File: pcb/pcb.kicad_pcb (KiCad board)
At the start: 2 copper layers, 95.2 x 71.1 mm, 14 parts, among them J1 encoder, J2 programmer, J3 oled display, J4 usb-ttl, SW1 reset, U1 ATmega32-16P

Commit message: actualizacion de pcb
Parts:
- added R3: 330, Resistor_THT:R_Axial_DIN0207_L6.3mm_D2.5mm_P7.62mm_Horizontal, F.Cu at (131.0, 73.0)
- added R4: 330, Resistor_THT:R_Axial_DIN0207_L6.3mm_D2.5mm_P7.62mm_Horizontal, F.Cu at (113.0, 72.8)
- added R5: 330, Resistor_THT:R_Axial_DIN0207_L6.3mm_D2.5mm_P7.62mm_Horizontal, F.Cu at (149.0, 72.8)
- added SW2: play/pause, Button_Switch_THT:SW_PUSH_6mm, F.Cu at (120.5, 66.8)
- added SW3: prev track, Button_Switch_THT:SW_PUSH_6mm, F.Cu at (101.8, 66.8)
- added SW4: next track, Button_Switch_THT:SW_PUSH_6mm, F.Cu at (138.5, 66.8)
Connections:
- J1 pad 3: unconnected-(J1-Pin_3-Pad3) -> Net-(J1-Pin_3)
- U1 pad 18: unconnected-(U1-PD4-Pad18) -> Net-(J1-Pin_3)
- U1 pad 21: unconnected-(U1-PD7-Pad21) -> Net-(U1-PD7)
- U1 pad 22: unconnected-(U1-PC0-Pad22) -> Net-(U1-PC0)
- U1 pad 23: unconnected-(U1-PC1-Pad23) -> Net-(U1-PC1)
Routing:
- net +5V: track 146.0 -> 213.8 mm
- net Net-(U1-PC1): track 0.00 -> 48.6 mm
- net Net-(U1-PC0): track 0.00 -> 32.4 mm
- net Net-(U1-PD7): track 0.00 -> 23.4 mm
- net Net-(J1-Pin_3): track 0.00 -> 18.0 mm

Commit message: add oled footprint
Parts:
- removed J3: oled display, Connector_PinHeader_2.54mm:PinHeader_1x20_P2.54mm_Vertical
- added DS1: NHD-0420CW-AG3, Library:NHD-0420CW-AG3, F.Cu at (107.3, 107.2)
- moved REF** 140.6 mm to (302.9, 143.9)
- moved REF** 140.3 mm to (304.1, 65.9)
- moved C1 108.4 mm to (237.6, 112.7)
- moved D1 108.4 mm to (265.5, 120.3)
- moved J1 108.4 mm to (255.3, 120.3)
- moved J4 108.4 mm to (245.2, 122.9)
- moved R3 108.4 mm to (239.0, 81.6)
- moved R4 108.4 mm to (221.0, 81.4)
- moved SW1 108.4 mm to (210.7, 128.2)
- moved SW2 108.4 mm to (228.5, 75.3)
- moved SW3 108.4 mm to (209.8, 75.3)
- moved SW4 108.4 mm to (246.5, 75.3)
- moved U1 108.4 mm to (209.6, 108.5)
- moved J2 108.4 mm to (222.3, 112.7)
- moved R2 108.4 mm to (232.5, 126.7)
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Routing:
- removed copper zone on B.Cu, net GND
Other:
- board size 95.2 x 71.1 mm -> 295 x 93 mm

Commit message: actualizacion de archivos con footprint OLED
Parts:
- moved J1 27.8 mm to (264.2, 94.0)
- moved REF** 4.67 mm to (19.9, 63.9)
- moved J2 4.20 mm to (218.4, 114.3)
- moved U1 3.95 mm to (205.7, 109.2)
- moved REF** 3.74 mm to (304.3, 147.3)
- moved DS1 3.55 mm to (110.5, 105.7)
- moved REF** 2.94 mm to (20.3, 146.9)
- moved D1 2.09 mm to (264.2, 121.9)
- moved C1 2.00 mm to (238.8, 114.3)
- moved J4 2.00 mm to (246.4, 124.5)
- moved REF** 1.98 mm to (304.4, 63.9)
- moved R2 1.64 mm to (231.1, 125.7)
- moved R3 1.59 mm to (238.7, 80.0)
- moved R1 1.52 mm to (259.1, 111.8)
- moved R4 1.41 mm to (220.7, 80.0)
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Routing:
- net Net-(DS1-~{CS}): track 20.3 -> 116.6 mm
- net Net-(DS1-DB1): track 35.3 -> 114.0 mm
- net Net-(DS1-DB0): track 38.5 -> 114.0 mm
- net +5V: track 213.8 -> 279.2 mm
- net GND: track 22.8 -> 0.00 mm
- net Net-(J1-Pin_3): track 18.0 -> 25.7 mm
- net Net-(J2-Pin_4): track 58.1 -> 54.2 mm
- net Net-(D1-A): track 5.08 -> 8.67 mm
- net Net-(J4-Pin_2): track 14.4 -> 17.3 mm
- net Net-(J4-Pin_1): track 14.4 -> 17.3 mm
- net Net-(U1-PC1): track 48.6 -> 45.8 mm
- net Net-(J1-Pin_5): track 25.1 -> 22.4 mm
- net Net-(U1-PC0): track 32.4 -> 29.8 mm
- net Net-(U1-PD7): track 23.4 -> 25.9 mm
- net Net-(U1-PD6): track 4.21 -> 6.13 mm
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
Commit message: actualizacion de archivos con footprint OLED
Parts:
- moved DS1 32.5 mm to (85.1, 85.4)
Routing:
- net Net-(DS1-~{CS}): track 116.6 -> 150.4 mm
- net Net-(DS1-DB1): track 114.0 -> 147.9 mm
- net Net-(DS1-DB0): track 114.0 -> 147.9 mm
- net +5V: track 279.2 -> 302.0 mm
- added copper zone on B.Cu, net GND
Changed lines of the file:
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@@
   )
   (footprint "Library:NHD-0420CW-AG3" (layer "F.Cu")
-    (at 110.49 105.69)
+    (at 85.09 85.37)
     (property "MANUFACTURER" "Newhaven Display")
     (property "MAXIMUM_PACKAGE_HEIGHT" "7.0 mm")
@@
   (segment (start 266.7 116.84) (end 264.16 119.38) (width 0.8) (layer "B.Cu") (net 3))
   (segment (start 266.7 111.76) (end 266.7 116.84) (width 0.8) (layer "B.Cu") (net 3))
-  (segment (start 127 93.98) (end 99.06 93.98) (width 0.8) (layer "F.Cu") (net 4))
   (segment (start 226.06 77.8) (end 220.65 72.39) (width 0.8) (layer "F.Cu") (net 4))
-  (segment (start 129.54 91.44) (end 127 93.98) (width 0.8) (layer "F.Cu") (net 4))
+  (segment (start 72.545 69.695) (end 102.715 69.695) (width 0.8) (layer "F.Cu") (net 4))
   (segment (start 226.06 86.36) (end 226.06 77.8) (width 0.8) (layer "F.Cu") (net 4))
-  (segment (start 99.06 93.98) (end 96.52 91.44) (width 0.8) (layer "F.Cu") (net 4))
+  (segment (start 71.12 71.12) (end 72.545 69.695) (width 0.8) (layer "F.Cu") (net 4))
   (segment (start 231.14 93.98) (end 231.14 91.44) (width 0.8) (layer "F.Cu") (net 4))
   (segment (start 226.06 93.98) (end 226.06 77.8) (width 0.8) (layer "F.Cu") (net 4))
   (segment (start 231.14 91.44) (end 226.06 86.36) (width 0.8) (layer "F.Cu") (net 4))
+  (segment (start 102.715 69.695) (end 104.14 71.12) (width 0.8) (layer "F.Cu") (net 4))
   (segment (start 226.06 106.68) (end 228.6 109.22) (width 0.8) (layer "B.Cu") (net 4))
   (segment (start 264.16 96.52) (end 262.957919 96.52) (width 0.8) (layer "B.Cu") (net 4))
   (segment (start 228.6 109.22) (end 228.6 115.57) (width 0.8) (layer "B.Cu") (net 4))
   (segment (start 226.06 93.98) (end 226.06 106.68) (width 0.8) (layer "B.Cu") (net 4))
+  (segment (start 220.65 72.39) (end 216.84 68.58) (width 0.8) (layer "B.Cu") (net 4))
+  (segment (start 106.68 68.58) (end 109.22 68.58) (width 0.8) (layer "B.Cu") (net 4))
   (segment (start 259.08 74.82) (end 256.65 72.39) (width 0.8) (layer "B.Cu") (net 4))
-  (segment (start 151.13 72.39) (end 220.65 72.39) (width 0.8) (layer "B.Cu") (net 4))
   (segment (start 234.95 118.11) (end 241.3 124.46) (width 0.8) (layer "B.Cu") (net 4))
-  (segment (start 132.08 91.44) (end 129.54 91.44) (width 0.8) (layer "B.Cu") (net 4))
   (segment (start 238.65 72.39) (end 256.65 72.39) (width 0.8) (layer "B.Cu") (net 4))
   (segment (start 238.65 72.39) (end 220.65 72.39) (width 0.8) (layer "B.Cu") (net 4))
+  (segment (start 104.14 71.12) (end 106.68 68.58) (width 0.8) (layer "B.Cu") (net 4))
+  (segment (start 216.84 68.58) (end 109.22 68.58) (width 0.8) (layer "B.Cu") (net 4))
+  (segment (start 109.22 68.58) (end 106.68 71.12) (width 0.8) (layer "B.Cu") (net 4))
   (segment (start 231.14 118.11) (end 234.95 118.11) (width 0.8) (layer "B.Cu") (net 4))
   (segment (start 262.957919 96.52) (end 259.08 92.642081) (width 0.8) (layer "B.Cu") (net 4))
   (segment (start 228.6 115.57) (end 231.14 118.11) (width 0.8) (layer "B.Cu") (net 4))
   (segment (start 259.08 92.642081) (end 259.08 74.82) (width 0.8) (layer "B.Cu") (net 4))
-  (segment (start 132.08 91.44) (end 151.13 72.39) (width 0.8) (layer "B.Cu") (net 4))
   (segment (start 266.7 103.65061) (end 266.7 101.6) (width 0.8) (layer "F.Cu") (net 5))
   (segment (start 266.7 101.6) (end 264.16 99.06) (width 0.8) (layer "F.Cu") (net 5))
@@
   (segment (start 252.65 78.74) (end 255.09 78.74) (width 0.8) (layer "B.Cu") (net 21))
   (segment (start 246.15 78.74) (end 252.65 78.74) (width 0.8) (layer "B.Cu") (net 21))
-  (segment (start 208.28 96.52) (end 220.98 109.22) (width 0.8) (layer "B.Cu") (net 36))
-  (segment (start 124.46 96.52) (end 208.28 96.52) (width 0.8) (layer "B.Cu") (net 36))
-  (segment (start 119.38 91.44) (end 124.46 96.52) (width 0.8) (layer "B.Cu") (net 36))
+  (segment (start 207.14 95.38) (end 220.98 109.22) (width 0.8) (layer "B.Cu") (net 36))
+  (segment (start 93.98 71.12) (end 118.24 95.38) (width 0.8) (layer "B.Cu") (net 36))
+  (segment (start 118.24 95.38) (end 207.14 95.38) (width 0.8) (layer "B.Cu") (net 36))
   (segment (start 220.98 109.22) (end 220.98 114.3) (width 0.8) (layer "B.Cu") (net 36))
-  (segment (start 218.44 109.22) (end 208.28 99.06) (width 0.8) (layer "B.Cu") (net 37))
+  (segment (start 213.36 104.14) (end 218.44 109.22) (width 0.8) (layer "B.Cu") (net 37))
   (segment (start 218.44 109.22) (end 218.44 114.3) (width 0.8) (layer "B.Cu") (net 37))
-  (segment (start 208.28 99.06) (end 124.46 99.06) (width 0.8) (layer "B.Cu") (net 37))
-  (segment (start 124.46 99.06) (end 116.84 91.44) (width 0.8) (layer "B.Cu") (net 37))
-  (segment (start 200.66 101.6) (end 208.28 109.22) (width 0.8) (layer "B.Cu") (net 38))
-  (segment (start 99.06 91.44) (end 109.22 101.6) (width 0.8) (layer "B.Cu") (net 38))
-  (segment (start 109.22 101.6) (end 200.66 101.6) (width 0.8) (layer "B.Cu") (net 38))
+  (segment (start 124.46 104.14) (end 213.36 104.14) (width 0.8) (layer "B.Cu") (net 37))
+  (segment (start 91.44 71.12) (end 124.46 104.14) (width 0.8) (layer "B.Cu") (net 37))
+  (segment (start 206.88 107.82) (end 208.28 109.22) (width 0.8) (layer "B.Cu") (net 38))
+  (segment (start 110.36 107.82) (end 206.88 107.82) (width 0.8) (layer "B.Cu") (net 38))
+  (segment (start 73.66 71.12) (end 110.36 107.82) (width 0.8) (layer "B.Cu") (net 38))
+  (zone (net 2) (net_name "GND") (layer "B.Cu") (hatch edge 0.5)
+    (connect_pads (clearance 0.5))
+    (min_thickness 0.25) (filled_areas_thickness no)
+    (fill yes (thermal_gap 0.5) (thermal_bridge_width 0.5))
+    (polygon
+      (pts
+        (xy 15.24 60.96)
+        (xy 309.88 60.96)
+        (xy 309.88 149.86)
+        (xy 15.24 149.86)
+      )
+    )
+  )
 )

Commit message: update pcb
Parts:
- J1: value encoder -> ENCODER
- J2: value programmer -> PROGRAMMER
- J4: value usb-ttl -> USB-TTL
- NEXT TRACK: renamed from SW4
- OLED DISPLAY: renamed from DS1
- PREV TRACK: renamed from SW3
- moved REF** 69.9 mm to (236.6, 130.0)
- moved REF** 68.1 mm to (236.7, 71.6)
- moved RESET 47.7 mm to (163.7, 120.0)
- moved D1 38.1 mm to (226.1, 121.9)
- moved J1 38.1 mm to (226.1, 94.0)
- moved U1 38.1 mm to (167.6, 109.2)
- moved C1 38.1 mm to (200.7, 114.3)
- moved J2 38.1 mm to (180.3, 114.3)
- moved J4 38.1 mm to (208.3, 124.5)
- moved NEXT TRACK 38.1 mm to (208.1, 74.2)
- moved PLAY/PAUSE 38.1 mm to (190.1, 74.2)
- moved PREV TRACK 38.1 mm to (171.3, 74.2)
- moved R1 38.1 mm to (221.0, 111.8)
- moved R2 38.1 mm to (193.0, 125.7)
- moved R3 38.1 mm to (200.6, 80.0)
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- renumbered SW2 to PLAY/PAUSE, SW1 to RESET
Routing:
- net +5V: track 302.0 -> 203.7 mm
- net Net-(DS1-~{CS}): track 150.4 -> 87.8 mm
- net Net-(DS1-DB1): track 147.9 -> 85.2 mm
- net Net-(DS1-DB0): track 147.9 -> 85.2 mm
- net Net-(J2-Pin_4): track 54.2 -> 59.8 mm
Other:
- board size 295 x 93 mm -> 199.8 x 72.9 mm
- board text added: "GND"
- board text added: "VTG"
- board text added: "https://github.com/rattamayhorka/vumeter"
- board text removed: "Designed by rattamayhorka 2023"

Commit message: update pcb
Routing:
- net +5V: track 203.7 -> 239.1 mm
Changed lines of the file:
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@@
       (drillshape 0)
       (scaleselection 1)
-      (outputdirectory "vumeter_pcb")
+      (outputdirectory "../../../Descargas/")
     )
   )
@@
   (segment (start 228.6 116.84) (end 226.06 119.38) (width 0.8) (layer "B.Cu") (net 3))
   (segment (start 228.6 111.76) (end 228.6 116.84) (width 0.8) (layer "B.Cu") (net 3))
+  (segment (start 125.375 69.215) (end 128.27 72.11) (width 0.8) (layer "F.Cu") (net 4))
   (segment (start 187.96 77.8) (end 182.55 72.39) (width 0.8) (layer "F.Cu") (net 4))
   (segment (start 187.96 86.36) (end 187.96 77.8) (width 0.8) (layer "F.Cu") (net 4))
+  (segment (start 98.145 69.215) (end 125.375 69.215) (width 0.8) (layer "F.Cu") (net 4))
   (segment (start 193.04 93.98) (end 193.04 91.44) (width 0.8) (layer "F.Cu") (net 4))
   (segment (start 187.96 93.98) (end 187.96 77.8) (width 0.8) (layer "F.Cu") (net 4))
   (segment (start 193.04 91.44) (end 187.96 86.36) (width 0.8) (layer "F.Cu") (net 4))
+  (segment (start 95.25 72.11) (end 98.145 69.215) (width 0.8) (layer "F.Cu") (net 4))
   (segment (start 187.96 106.68) (end 190.5 109.22) (width 0.8) (layer "B.Cu") (net 4))
   (segment (start 226.06 96.52) (end 224.857919 96.52) (width 0.8) (layer "B.Cu") (net 4))

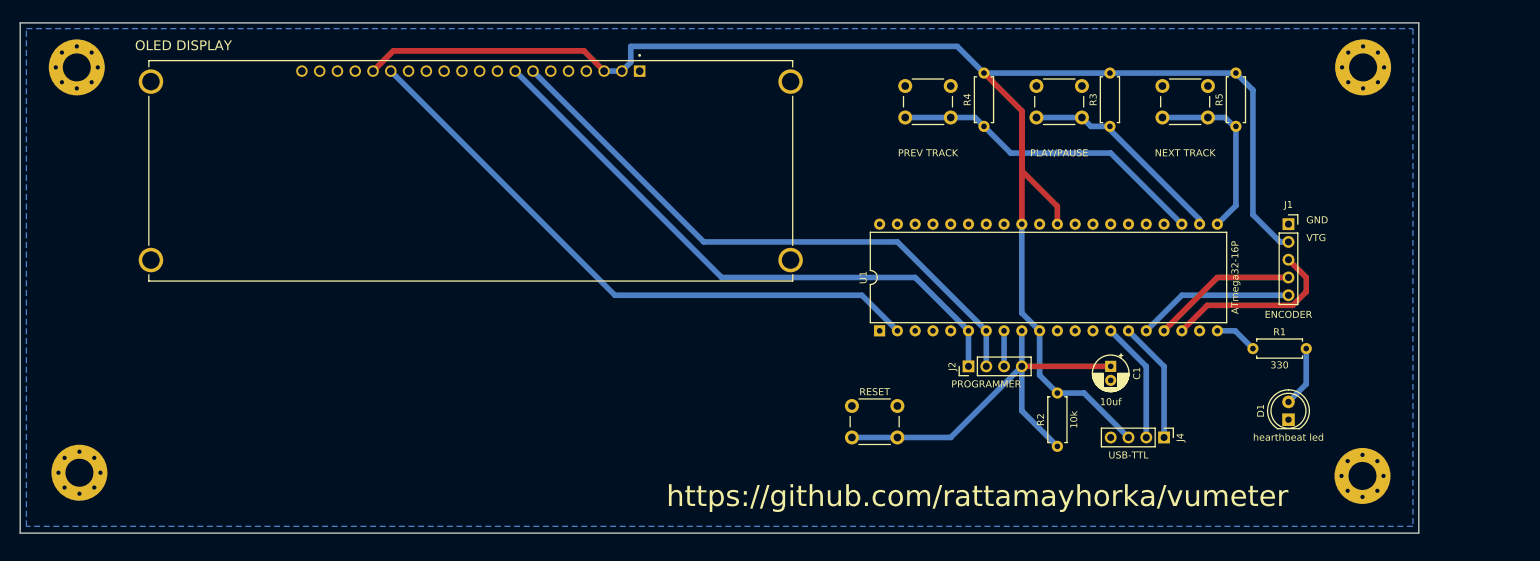
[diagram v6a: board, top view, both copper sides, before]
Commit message: agrego timer de apagado si no hay conexion a pc
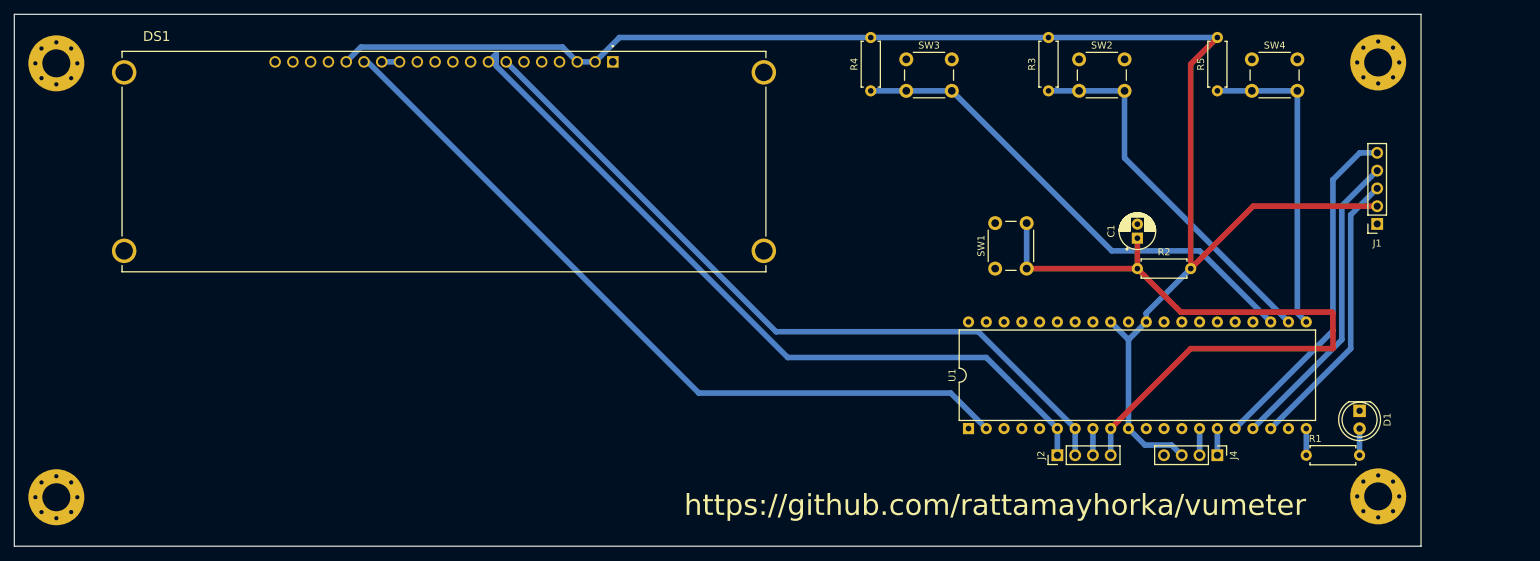
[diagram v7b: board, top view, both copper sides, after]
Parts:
- removed NEXT TRACK: next track, Button_Switch_THT:SW_PUSH_6mm
- removed OLED DISPLAY: NHD-0420CW-AG3, Library:NHD-0420CW-AG3
- removed PLAY/PAUSE: play/pause, Button_Switch_THT:SW_PUSH_6mm
- removed PREV TRACK: prev track, Button_Switch_THT:SW_PUSH_6mm
- removed the REF** at (53.3, 129.5)
- removed the REF** at (236.7, 71.6)
- removed the REF** at (236.6, 130.0)
- removed RESET: reset, Button_Switch_THT:SW_PUSH_6mm
- added DS1: NHD-0420CW-AG3, Library:NHD-0420CW-AG3, F.Cu at (105.4, 85.0)
- added REF**: MountingHole_4mm_Pad_Via, MountingHole:MountingHole_4mm_Pad_Via, F.Cu at (238.9, 70.9)
- added REF**: MountingHole_4mm_Pad_Via, MountingHole:MountingHole_4mm_Pad_Via, F.Cu at (50.0, 133.0)
- added REF**: MountingHole_4mm_Pad_Via, MountingHole:MountingHole_4mm_Pad_Via, F.Cu at (238.9, 132.9)
- added SW1: reset, Button_Switch_THT:SW_PUSH_6mm, F.Cu at (184.2, 100.3)
- added SW2: play/pause, Button_Switch_THT:SW_PUSH_6mm, F.Cu at (196.1, 70.4)
- added SW3: prev track, Button_Switch_THT:SW_PUSH_6mm, F.Cu at (171.4, 70.4)
- added SW4: next track, Button_Switch_THT:SW_PUSH_6mm, F.Cu at (220.8, 70.4)
- J1: value ENCODER -> encoder
- J2: value PROGRAMMER -> programmer
- J4: value USB-TTL -> usb-ttl
- moved R2 27.9 mm to (204.5, 100.3), turned to 0 degrees
- moved U1 18.9 mm to (180.3, 123.2)
- moved C1 18.7 mm to (204.5, 96.0), turned to 90 degrees
- moved J2 18.0 mm to (193.0, 127.0)
- moved R1 17.0 mm to (228.6, 127.0)
- moved R4 17.0 mm to (166.4, 74.9)
- moved J1 12.7 mm to (238.7, 94.0), turned to 180 degrees
- moved D1 10.2 mm to (236.2, 120.7), turned to -90 degrees
- moved R3 10.1 mm to (191.8, 74.9)
- moved J4 8.02 mm to (215.9, 127.0)
- moved R5 5.73 mm to (215.9, 74.9)
- moved REF** 2.98 mm to (50.0, 71.0)
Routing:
- net Net-(J2-Pin_4): track 59.8 -> 102.6 mm
- net Net-(J1-Pin_5): track 22.4 -> 49.3 mm
- net Net-(U1-PC1): track 45.8 -> 70.8 mm
- net Net-(U1-PC0): track 29.8 -> 53.6 mm
- net Net-(DS1-DB1): track 85.2 -> 108.7 mm
- net Net-(J1-Pin_4): track 20.9 -> 44.2 mm
- net Net-(DS1-~{CS}): track 87.8 -> 110.6 mm
- net Net-(DS1-DB0): track 85.2 -> 106.8 mm
- net Net-(U1-PD7): track 25.9 -> 45.0 mm
- net Net-(J1-Pin_3): track 25.7 -> 40.6 mm
- net Net-(J4-Pin_2): track 17.3 -> 3.81 mm
- net Net-(J4-Pin_1): track 17.3 -> 3.81 mm
- net +5V: track 239.1 -> 231.9 mm
- net Net-(D1-A): track 8.67 -> 3.81 mm
- net GND: track 0.00 -> 2.54 mm
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- removed copper zone on B.Cu, net GND
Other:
- board size 199.8 x 72.9 mm -> 201 x 76 mm
- board text removed: "GND"
- board text removed: "VTG"

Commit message: retomando proyecto
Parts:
- added REF**: Encoder_module, encoder:Encoder_module, F.Cu at (225.1, 89.1)
- moved SW1 46.6 mm to (219.6, 130.5), turned to 0 degrees
- moved C1 36.5 mm to (199.4, 132.1), turned to 180 degrees
- moved R2 31.8 mm to (203.2, 132.1)
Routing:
- net Net-(J2-Pin_4): track 102.6 -> 31.4 mm
- net +5V: track 231.9 -> 167.2 mm
